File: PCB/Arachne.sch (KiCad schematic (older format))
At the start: 36 parts, among them SW101 SW_Push, U101 STM32L452CEUx, U102 WS2818B

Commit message: PCB:
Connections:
- net BUSY_1: now also RN101.7 (R2.2); no longer RN101.8 (R1.2)
- net FLAG_1: now also RN101.8 (R1.2); no longer RN101.7 (R2.2)
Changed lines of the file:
@@
 Text Label 8000 2200 1    50   ~ 0
 FLAG_2
-Text Label 8100 2200 1    50   ~ 0
-BUSY_2
 Wire Wire Line
 	8575 2300 9150 2300
@@
 Wire Wire Line
 	8300 1200 8300 1550
+Text Label 8300 2200 1    50   ~ 0
+FLAG_1
+Wire Wire Line
+	8200 1950 8200 2200
+Wire Wire Line
+	8300 1950 8300 2200
 Text Label 8200 2200 1    50   ~ 0
-FLAG_1
-Wire Wire Line
-	8200 1950 8200 2200
-Wire Wire Line
-	8300 1950 8300 2200
-Text Label 8300 2200 1    50   ~ 0
 BUSY_1
 Wire Wire Line
@@
 	1    0    0    -1
 $EndComp
+Text Label 8100 2200 1    50   ~ 0
+BUSY_2
 $EndSCHEMATC

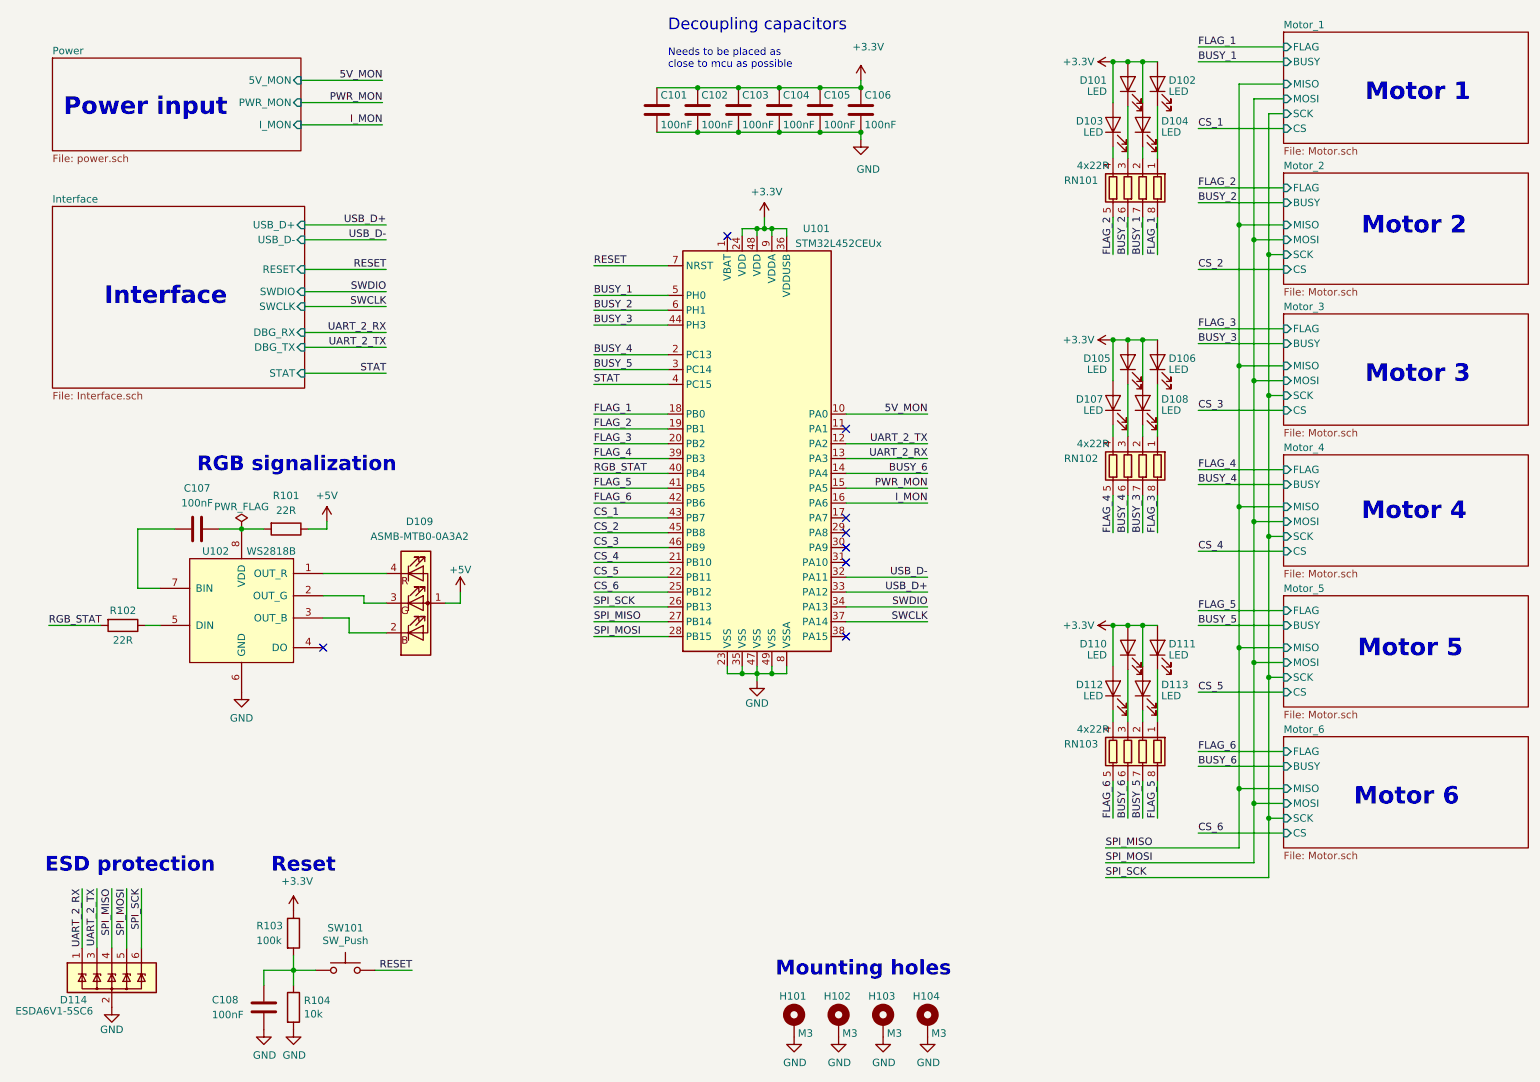
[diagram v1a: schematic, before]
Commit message: Schema: add Salae debug IDC connector
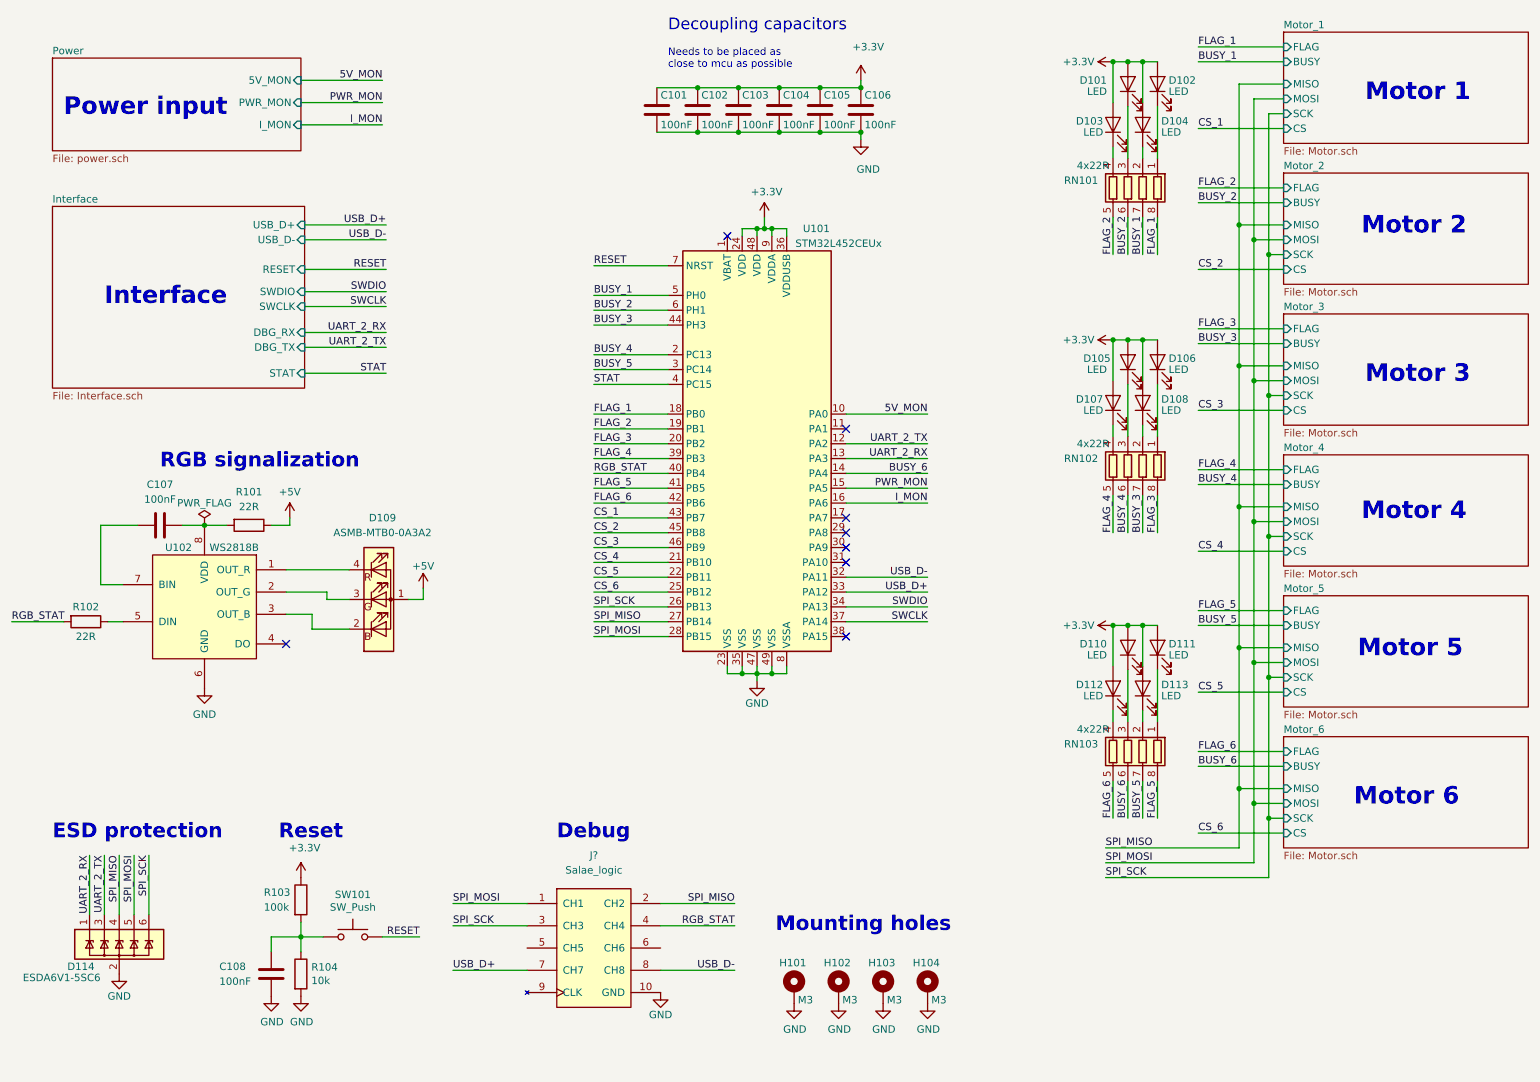
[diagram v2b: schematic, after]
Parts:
- added J?: Salae_logic, Connector_IDC:IDC-Header_2x05_P2.54mm_Horizontal, symbol TCY_connectors:Salae_logic
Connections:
- net GND: now also J?.10 (GND)
- net RGB_STAT: now also J?.4 (CH4)
- net SPI_MISO: now also J?.2 (CH2)
- net SPI_MOSI: now also J?.1 (CH1)
- net SPI_SCK: now also J?.3 (CH3)
- net USB_D+: now also J?.7 (CH7)
- net USB_D-: now also J?.8 (CH8)
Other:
- note added: "Debug\n"
- moved on the sheet: C107, C108, D109, D114, H101, H102, H103, H104, R101, R102, R103, R104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

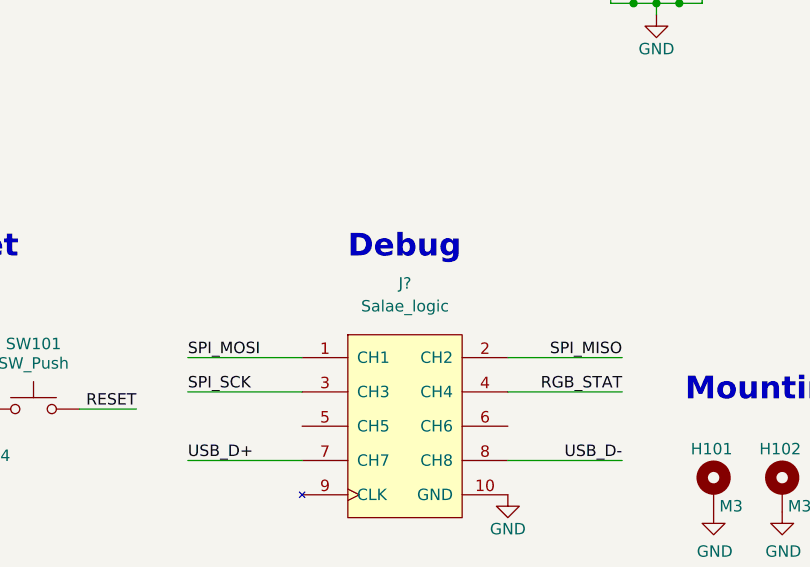
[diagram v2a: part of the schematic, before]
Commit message: PCB: change programing and debugging IDC connectors to vertical version
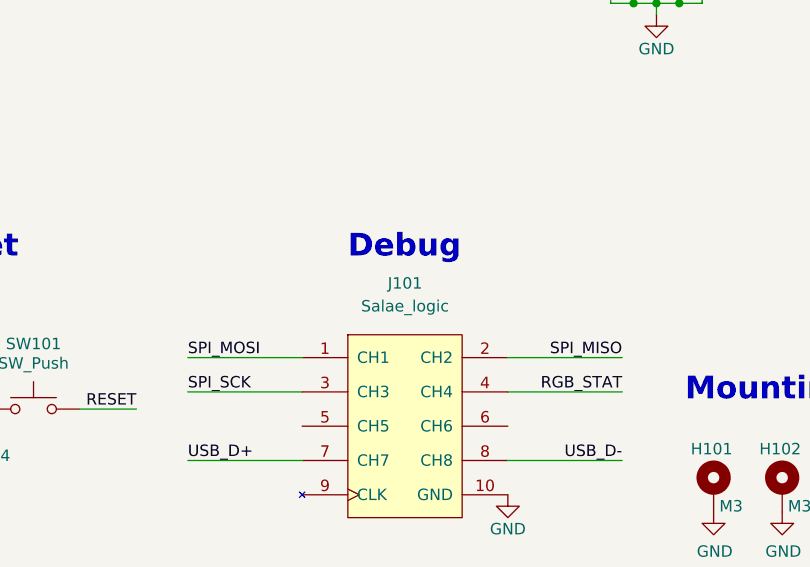
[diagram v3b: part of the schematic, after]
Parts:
- J101: renamed from J?; footprint Connector_IDC:IDC-Header_2x05_P2.54mm_Horizontal -> Connector_IDC:IDC-Header_2x05_P2.54mm_Vertical
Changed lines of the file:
@@
 	4500 4775 5000 4775
 $Comp
-L TCY_connectors:Salae_logic J?
+L TCY_connectors:Salae_logic J101
 U 1 1 5E6544A4
 P 4500 6725
-F 0 "J?" H 4500 7200 50  0000 C CNN
+F 0 "J101" H 4500 7200 50  0000 C CNN
 F 1 "Salae_logic" H 4500 7100 50  0000 C CNN
-F 2 "Connector_IDC:IDC-Header_2x05_P2.54mm_Horizontal" H 4300 7125 50  0001 C CNN
+F 2 "Connector_IDC:IDC-Header_2x05_P2.54mm_Vertical" H 4300 7125 50  0001 C CNN
 F 3 "" H 4300 7125 50  0001 C CNN
 	1    4500 6725
@@
 USB_D-
 $Comp
-L power:GND #PWR?
+L power:GND #PWR0119
 U 1 1 5E725F83
 P 4950 7175
-F 0 "#PWR?" H 4950 6925 50  0001 C CNN
+F 0 "#PWR0119" H 4950 6925 50  0001 C CNN
 F 1 "GND" H 4950 7025 50  0000 C CNN
 F 2 "" H 4950 7175 50  0001 C CNN
